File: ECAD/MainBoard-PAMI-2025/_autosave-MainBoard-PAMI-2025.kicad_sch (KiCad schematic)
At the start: 67 parts, among them J1 Sensor_Center, J10 Serial, J11 Con_Batt, J13 OLED, J2 USB_B, J3 Sensor_RIGHT, J4 Servo, J5 Sensor_LEFT, J6 Servo, J7 LeftMotor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

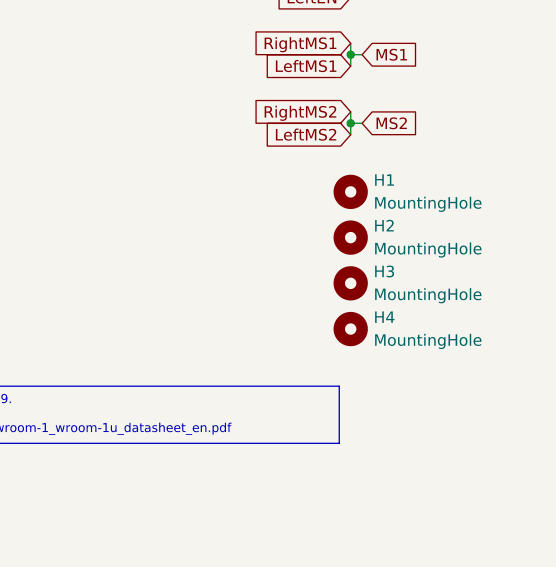
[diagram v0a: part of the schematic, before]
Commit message: New halle effect sensor for tirette
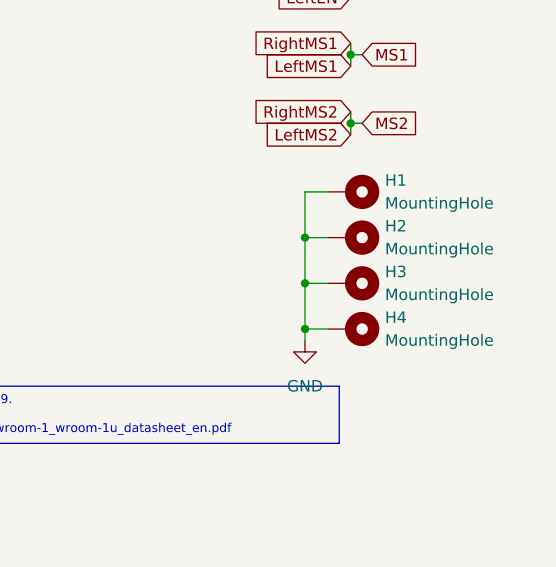
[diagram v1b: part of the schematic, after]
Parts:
- H1, H2, H3, H4: footprint MountingHole:MountingHole_3.2mm_M3 -> MountingHole:MountingHole_3.2mm_M3_Pad_Via; symbol Mechanical:MountingHole -> Mechanical:MountingHole_Pad; now left out of the parts list
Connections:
- net GND: now also H1.1, H2.1, H3.1, H4.1
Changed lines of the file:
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@@
 	)
 	(junction
+		(at 261.62 156.21)
+		(diameter 0)
+		(color 0 0 0 0)
+	)
+	(junction
 		(at 57.15 87.63)
 		(diameter 0)
@@
 	)
 	(junction
+		(at 261.62 151.13)
+		(diameter 0)
+		(color 0 0 0 0)
+	)
+	(junction
 		(at 266.7 130.81)
 		(diameter 0)
@@
 		(color 0 0 0 0)
 	)
+	(junction
+		(at 261.62 161.29)
+		(diameter 0)
+		(color 0 0 0 0)
+	)
 	(no_connect
 		(at 236.22 105.41)
@@
 	(wire
 		(pts
+			(xy 264.16 146.05) (xy 261.62 146.05)
+		)
+		(stroke
+			(width 0)
+			(type default)
+		)
+	)
+	(wire
+		(pts
 			(xy 207.01 26.67) (xy 210.82 26.67)
 		)
@@
 	(wire
 		(pts
+			(xy 261.62 161.29) (xy 261.62 162.56)
+		)
+		(stroke
+			(width 0)
+			(type default)
+		)
+	)
+	(wire
+		(pts
 			(xy 26.67 121.92) (xy 27.94 121.92)
 		)
@@
 	(wire
 		(pts
+			(xy 261.62 151.13) (xy 264.16 151.13)
+		)
+		(stroke
+			(width 0)
+			(type default)
+		)
+	)
+	(wire
+		(pts
 			(xy 49.53 87.63) (xy 49.53 92.71)
 		)
@@
 	(wire
 		(pts
+			(xy 261.62 156.21) (xy 261.62 161.29)
+		)
+		(stroke
+			(width 0)
+			(type default)
+		)
+	)
+	(wire
+		(pts
 			(xy 266.7 129.54) (xy 266.7 130.81)
 		)
@@
 	(wire
 		(pts
+			(xy 261.62 151.13) (xy 261.62 156.21)
+		)
+		(stroke
+			(width 0)
+			(type default)
+		)
+	)
+	(wire
+		(pts
 			(xy 78.74 33.02) (xy 78.74 34.29)
 		)
@@
 	(wire
 		(pts
+			(xy 261.62 146.05) (xy 261.62 151.13)
+		)
+		(stroke
+			(width 0)
+			(type default)
+		)
+	)
+	(wire
+		(pts
 			(xy 158.75 163.83) (xy 158.75 167.64)
 		)
@@
 	(wire
 		(pts
+			(xy 261.62 156.21) (xy 264.16 156.21)
+		)
+		(stroke
+			(width 0)
+			(type default)
+		)
+	)
+	(wire
+		(pts
 			(xy 111.76 62.23) (xy 111.76 63.5)
 		)
@@
 	(wire
 		(pts
+			(xy 261.62 161.29) (xy 264.16 161.29)
+		)
+		(stroke
+			(width 0)
+			(type default)
+		)
+	)
+	(wire
+		(pts
 			(xy 66.04 57.15) (xy 66.04 58.42)
 		)
@@
 	)
 	(symbol
-		(lib_id "Mechanical:MountingHole")
-		(at 266.7 146.05 0)
+		(lib_id "Mechanical:MountingHole_Pad")
+		(at 266.7 146.05 270)
 		(unit 1)
-		(exclude_from_sim no)
-		(in_bom yes)
+		(exclude_from_sim yes)
+		(in_bom no)
 		(on_board yes)
 		(dnp no)
+		(fields_autoplaced yes)
 		(property "Reference" "H1"
-			(at 269.24 144.78 0)
+			(at 270.51 144.7799 90)
 			(effects
 				(font
@@
 		)
 		(property "Value" "MountingHole"
-			(at 269.24 147.32 0)
+			(at 270.51 147.3199 90)
 			(effects
 				(font
@@
 			)
 		)
-		(property "Footprint" "MountingHole:MountingHole_3.2mm_M3"
+		(property "Footprint" "MountingHole:MountingHole_3.2mm_M3_Pad_Via"
 			(at 266.7 146.05 0)
 			(effects
@@
 			)
 		)
-		(property "Description" ""
+		(property "Description" "Mounting Hole with connection"
 			(at 266.7 146.05 0)
 			(effects
@@
 			)
 		)
+		(pin "1"
+		)
 		(instances
 			(project "MainBoard-PAMI-2025"
@@
 	)
 	(symbol
-		(lib_id "Mechanical:MountingHole")
-		(at 266.7 156.21 0)
+		(lib_id "Mechanical:MountingHole_Pad")
+		(at 266.7 156.21 270)
 		(unit 1)
-		(exclude_from_sim no)
-		(in_bom yes)
+		(exclude_from_sim yes)
+		(in_bom no)
 		(on_board yes)
 		(dnp no)
+		(fields_autoplaced yes)
 		(property "Reference" "H3"
-			(at 269.24 154.94 0)
+			(at 270.51 154.9399 90)
 			(effects
 				(font
@@
 		)
 		(property "Value" "MountingHole"
-			(at 269.24 157.48 0)
+			(at 270.51 157.4799 90)
 			(effects
 				(font
@@
 			)
 		)
-		(property "Footprint" "MountingHole:MountingHole_3.2mm_M3"
+		(property "Footprint" "MountingHole:MountingHole_3.2mm_M3_Pad_Via"
 			(at 266.7 156.21 0)
 			(effects
@@
 			)
 		)
-		(property "Description" ""
+		(property "Description" "Mounting Hole with connection"
 			(at 266.7 156.21 0)
 			(effects
@@
 			)
 		)
+		(pin "1"
+		)
 		(instances
 			(project "MainBoard-PAMI-2025"
@@
 	)
 	(symbol
-		(lib_id "Mechanical:MountingHole")
-		(at 266.7 151.13 0)
+		(lib_id "Mechanical:MountingHole_Pad")
+		(at 266.7 151.13 270)
 		(unit 1)
-		(exclude_from_sim no)
-		(in_bom yes)
+		(exclude_from_sim yes)
+		(in_bom no)
 		(on_board yes)
 		(dnp no)
+		(fields_autoplaced yes)
 		(property "Reference" "H2"
-			(at 269.24 149.86 0)
+			(at 270.51 149.8599 90)
 			(effects
 				(font
@@
 		)
 		(property "Value" "MountingHole"
-			(at 269.24 152.4 0)
+			(at 270.51 152.3999 90)
 			(effects
 				(font
@@
 			)
 		)
-		(property "Footprint" "MountingHole:MountingHole_3.2mm_M3"
+		(property "Footprint" "MountingHole:MountingHole_3.2mm_M3_Pad_Via"
 			(at 266.7 151.13 0)
 			(effects
@@
 			)
 		)
-		(property "Description" ""
+		(property "Description" "Mounting Hole with connection"
 			(at 266.7 151.13 0)
 			(effects
@@
 			)
 		)
+		(pin "1"
+		)
 		(instances
 			(project "MainBoard-PAMI-2025"
@@
 	)
 	(symbol
-		(lib_id "Mechanical:MountingHole")
-		(at 266.7 161.29 0)
+		(lib_id "Mechanical:MountingHole_Pad")
+		(at 266.7 161.29 270)
 		(unit 1)
-		(exclude_from_sim no)
-		(in_bom yes)
+		(exclude_from_sim yes)
+		(in_bom no)
 		(on_board yes)
 		(dnp no)
+		(fields_autoplaced yes)
 		(property "Reference" "H4"
-			(at 269.24 160.02 0)
+			(at 270.51 160.0199 90)
 			(effects
 				(font
@@
 		)
 		(property "Value" "MountingHole"
-			(at 269.24 162.56 0)
+			(at 270.51 162.5599 90)
 			(effects
 				(font
@@
 			)
 		)
-		(property "Footprint" "MountingHole:MountingHole_3.2mm_M3"
+		(property "Footprint" "MountingHole:MountingHole_3.2mm_M3_Pad_Via"
 			(at 266.7 161.29 0)
 			(effects
@@
 			)
 		)
-		(property "Description" ""
+		(property "Description" "Mounting Hole with connection"
 			(at 266.7 161.29 0)
 			(effects
@@
 			)
 		)
+		(pin "1"
+		)
 		(instances
 			(project "MainBoard-PAMI-2025"
@@
 					(unit 1)
 				)
+			)
+		)
+	)
+	(symbol
+		(lib_id "power:GND")
+		(at 261.62 162.56 0)
+		(unit 1)
+		(exclude_from_sim no)
+		(in_bom yes)
+		(on_board yes)
+		(dnp no)
+		(fields_autoplaced yes)
+		(property "Reference" "#PWR064"
+			(at 261.62 168.91 0)
+			(effects
+				(font
+					(size 1.27 1.27)
+				)
+				(hide yes)
+			)
+		)
+		(property "Value" "GND"
+			(at 261.62 167.64 0)
+			(effects
+				(font
+					(size 1.27 1.27)
+				)
+			)
+		)
+		(property "Footprint" ""
+			(at 261.62 162.56 0)
+			(effects
+				(font
+					(size 1.27 1.27)
+				)
+				(hide yes)
+			)
+		)
+		(property "Datasheet" ""
+			(at 261.62 162.56 0)
+			(effects
+				(font
+					(size 1.27 1.27)
+				)
+				(hide yes)
+			)
+		)
+		(property "Description" ""
+			(at 261.62 162.56 0)
+			(effects
+				(font
+					(size 1.27 1.27)
+				)
+				(hide yes)
+			)
+		)
+		(pin "1"
+		)
+		(instances
+			(project "MainBoard-PAMI-2025"
+				(path "/d3e1aeb6-1412-4438-ac7d-372534bf2609"
+					(reference "#PWR064")
+					(unit 1)
+				)
